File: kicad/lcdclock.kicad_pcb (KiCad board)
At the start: 2 copper layers, 102 x 102 mm, 25 parts, among them CON1 AVR-ISP, SW1 RESET, U1 ATTINY24A, U2 AY0438, U3 AY0438, U4 LCD_DE377, U5 CONRAD_DCF, Y1 32.768kHz/12.5pF

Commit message: Route PCB
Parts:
- moved C4 99.1 mm to (70.7, 38.8), turned to 180 degrees
- moved C2 90.5 mm to (46.0, 54.5), turned to 270 degrees
- moved C3 54.9 mm to (123.2, 99.8), turned to 270 degrees
- moved SW1 52.9 mm to (128.5, 63.5), turned to 0 degrees
- moved TP1 44.1 mm to (60.8, 60.8)
- moved TP3 33.0 mm to (66.0, 60.8)
- moved TP2 31.1 mm to (71.2, 60.8)
- moved TP5 19.6 mm to (48.8, 95.2)
- moved U3 13.4 mm to (120.5, 98.2)
- moved U2 11.8 mm to (48.7, 56.2)
- moved C5 7.42 mm to (48.8, 86.0), turned to 90 degrees
- moved TP6 7.29 mm to (65.8, 77.2)
- moved TP4 6.77 mm to (46.0, 81.2)
- moved CON1 6.64 mm to (127.2, 72.8), turned to 270 degrees
- moved D1 4.24 mm to (50.0, 66.0)
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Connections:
- U1 pad 11: Net-(TP3-Pad1) -> Net-(TP2-Pad1)
- U1 pad 12: Net-(TP2-Pad1) -> Net-(TP3-Pad1)
- U4 pad 29: Net-(U3-Pad20) -> Net-(U3-Pad11)
- U4 pad 31: Net-(U3-Pad19) -> Net-(U3-Pad12)
- U4 pad 32: Net-(U3-Pad18) -> Net-(U3-Pad13)
- U4 pad 33: Net-(U3-Pad17) -> Net-(U3-Pad14)
- U4 pad 35: Net-(U3-Pad16) -> Net-(U3-Pad15)
- U4 pad 36: Net-(U3-Pad15) -> Net-(U3-Pad16)
- U4 pad 37: Net-(U3-Pad14) -> Net-(U3-Pad17)
- U4 pad 38: Net-(U3-Pad13) -> Net-(U3-Pad18)
- U4 pad 39: Net-(U3-Pad12) -> Net-(U3-Pad19)
- U4 pad 40: Net-(U3-Pad11) -> Net-(U3-Pad20)
- U4 pad 67: Net-(U2-Pad20) -> Net-(U2-Pad10)
- U4 pad 68: Net-(U2-Pad19) -> Net-(U2-Pad11)
- U4 pad 70: Net-(U2-Pad18) -> Net-(U2-Pad12)
- U4 pad 72: Net-(U2-Pad17) -> Net-(U2-Pad13)
- U4 pad 73: Net-(U2-Pad16) -> Net-(U2-Pad14)
- U4 pad 76: Net-(U2-Pad14) -> Net-(U2-Pad16)
- U4 pad 77: Net-(U2-Pad13) -> Net-(U2-Pad17)
- U4 pad 78: Net-(U2-Pad12) -> Net-(U2-Pad18)
- U4 pad 79: Net-(U2-Pad11) -> Net-(U2-Pad19)
- U4 pad 80: Net-(U2-Pad10) -> Net-(U2-Pad20)
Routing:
- net Net-(U3-Pad30): track 0.00 -> 220.6 mm, vias 0 -> 5
- net +BATT: track 4.19 -> 193.1 mm
- net Net-(TP3-Pad1): track 7.76 -> 134.0 mm, vias 0 -> 8
- net Net-(U2-Pad35): track 0.00 -> 102.2 mm, vias 0 -> 6
- net Net-(TP1-Pad1): track 0.00 -> 100.0 mm, vias 0 -> 4
- net Net-(U2-Pad30): track 0.00 -> 97.1 mm, vias 0 -> 4
- net Net-(CON1-Pad1): track 0.00 -> 55.3 mm
- net Net-(CON1-Pad4): track 0.00 -> 54.9 mm
- net Net-(CON1-Pad5): track 29.3 -> 83.7 mm, vias 0 -> 1
- net GND: track 2.00 -> 56.2 mm, vias 1 -> 9
- net Net-(TP2-Pad1): track 0.00 -> 53.6 mm
- net Net-(U3-Pad20): track 0.00 -> 49.5 mm
- net Net-(U3-Pad18): track 0.00 -> 49.5 mm
- net Net-(U3-Pad19): track 0.00 -> 49.5 mm
- net Net-(U3-Pad15): track 0.00 -> 49.5 mm
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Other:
- rule pad_to_mask_clearance: 0.2 -> 0.1

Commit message: Place components on PCB
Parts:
- removed C2: 100n, Resistors_SMD:R_0805_HandSoldering
- removed CON1: AVR-ISP, Connectors:IDC_Header_Straight_6pins
- removed R2, R3: 0, Resistors_SMD:R_0805_HandSoldering
- removed TP1: DLOA, Measurement_Points:Measurement_Point_Round-SMD-Pad_Big
- removed TP2: DDAT, Measurement_Points:Measurement_Point_Round-SMD-Pad_Big
- removed TP3: DCLK, Measurement_Points:Measurement_Point_Round-SMD-Pad_Big
- removed TP4: TVCC, Measurement_Points:Measurement_Point_Round-SMD-Pad_Big
- removed TP5: TSIG, Measurement_Points:Measurement_Point_Round-SMD-Pad_Big
- removed TP6: CLK, Measurement_Points:Measurement_Point_Round-SMD-Pad_Big
- removed U5: CONRAD_DCF, LCD Clock:CONNECTOR_4x1
- added C10: 100n, Resistors_SMD:R_0805_HandSoldering, F.Cu at (48.5, 56.5)
- added C11: 15p, Resistors_SMD:R_0805_HandSoldering, F.Cu at (21.8, 36.0)
- added C12: 15p, Resistors_SMD:R_0805_HandSoldering, F.Cu at (21.8, 44.0)
- added C13: 2.2u, Resistors_SMD:R_0805_HandSoldering, F.Cu at (49.0, 32.8)
- added C14: 1u, Resistors_SMD:R_0805_HandSoldering, F.Cu at (43.5, 32.8)
- added C6: 100n, Resistors_SMD:R_0805_HandSoldering, F.Cu at (38.5, 49.5)
- added C7: 100n, Resistors_SMD:R_0805_HandSoldering, F.Cu at (31.2, 35.0)
- added C8: 100n, Resistors_SMD:R_0805_HandSoldering, F.Cu at (29.2, 42.2)
- added C9: 1u, Resistors_SMD:R_0805_HandSoldering, F.Cu at (29.2, 47.0)
- added J1: Conn_JLink_SWD, Connectors:IDC_Header_Straight_20pins, F.Cu at (56.5, 55.6)
- BT1: value 3.6V Lithium AA -> 4xAA 6.4-3.2V
- C1: value 100n -> 10u
- C4: value 120p -> 100n
- D1: value BAT60A -> LED; footprint Diodes_SMD:D_SOD-323_HandSoldering -> LCD Clock:CONNECTOR_2x1
- L1: footprint LCD Clock:WE_470uH_Inductor -> Resistors_SMD:R_1812_HandSoldering
- R1: value 10k -> 100k
- SW1: value RESET -> SW_Push; footprint Buttons_Switches_SMD:SW_SPST_PTS645 -> Buttons_Switches_SMD:SW_SPST_B3S-1000
- U1: value ATTINY24A -> STM32L073xx_48; footprint Housings_SOIC:SOIC-14_3.9x8.7mm_Pitch1.27mm -> Housings_QFP:LQFP-48_7x7mm_Pitch0.5mm
- U2: value AY0438 -> ELV_DCF-2; footprint Housings_DIP:DIP-40_W15.24mm -> LCD Clock:CONNECTOR_3x1
- U3: value AY0438 -> TPS70630; footprint Housings_DIP:DIP-40_W15.24mm -> TO_SOT_Packages_SMD:SOT-23-5_HandSoldering
- U4: value LCD_DE377 -> LCD; footprint LCD Clock:LCD-DIP -> Connectors:IDC_Header_Straight_16pins; moved to F.Cu
- Y1: value 32.768kHz/12.5pF -> 32.768kHz 12.5pF; footprint LCD Clock:MS1V-T1K -> Crystals:Crystal_SMD_SeikoEpson_MC405-2pin_9.6x4.1mm_HandSoldering
- moved U3 101.0 mm to (46.0, 30.0)
- moved C3 99.9 mm to (44.0, 39.0), turned to 0 degrees
- moved SW1 73.5 mm to (55.0, 65.2)
- moved L1 61.7 mm to (40.5, 25.5), turned to 90 degrees
- moved C5 61.6 mm to (37.0, 25.5)
- moved U4 57.5 mm to (26.2, 65.5), turned to 0 degrees
- moved U1 55.3 mm to (36.0, 41.5)
- moved Y1 54.0 mm to (25.2, 40.0), turned to 270 degrees
- moved C1 51.3 mm to (40.8, 34.5), turned to 270 degrees
- moved BT1 46.3 mm to (46.8, 22.2), turned to 270 degrees
- moved R1 43.2 mm to (37.0, 55.5), turned to 270 degrees
- moved C4 37.5 mm to (33.5, 33.5), turned to 90 degrees
- moved U2 32.3 mm to (34.2, 27.3)
- moved D1 18.4 mm to (34.2, 56.5), turned to 90 degrees
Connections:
- C1 pad 1: +BATT -> VCC
- C3 pad 1: +BATT -> VCC
- C4 pad 1: Net-(C4-Pad1) -> VCC
- D1 pad 1: +BATT -> GND
- D1 pad 2: Net-(BT1-Pad1) -> Net-(D1-Pad2)
- R1 pad 1: +BATT -> Net-(D1-Pad2)
- R1 pad 2: Net-(CON1-Pad5) -> Net-(R1-Pad2)
- SW1 pad 2: Net-(CON1-Pad5) -> Net-(C10-Pad2)
- U1 pad 1: +BATT -> VCC
- U1 pad 10: Net-(TP5-Pad1) -> (no net)
- U1 pad 11: Net-(TP2-Pad1) -> Net-(U1-Pad11)
- U1 pad 12: Net-(TP3-Pad1) -> Net-(U1-Pad12)
- U1 pad 13: Net-(TP1-Pad1) -> Net-(U1-Pad13)
- U1 pad 14: GND -> Net-(L1-Pad1)
- U1 pad 2: Net-(R3-Pad2) -> (no net)
- U1 pad 3: Net-(R2-Pad2) -> Net-(C11-Pad1)
- U1 pad 4: Net-(CON1-Pad5) -> Net-(C12-Pad1)
- U1 pad 5: Net-(TP6-Pad1) -> (no net)
- U1 pad 6: Net-(L1-Pad1) -> (no net)
- U1 pad 7: Net-(CON1-Pad4) -> Net-(C10-Pad2)
- U1 pad 8: Net-(CON1-Pad1) -> GND
- U1 pad 9: Net-(CON1-Pad3) -> VCC
- U2 pad 1: +BATT -> Net-(C5-Pad2)
- U2 pad 2: Net-(TP1-Pad1) -> Net-(U1-Pad15)
- U2 pad 3: (no net) -> GND
- U3 pad 1: +BATT -> Net-(BT1-Pad1)
- U3 pad 2: Net-(TP1-Pad1) -> GND
- U3 pad 3: (no net) -> Net-(BT1-Pad1)
- U3 pad 5: (no net) -> VCC
- U4 pad 1: Net-(U3-Pad30) -> Net-(U1-Pad11)
- U4 pad 10: Net-(U3-Pad27) -> Net-(U1-Pad41)
- U4 pad 11: Net-(U3-Pad26) -> Net-(U1-Pad21)
- U4 pad 12: Net-(U3-Pad25) -> Net-(U1-Pad22)
- U4 pad 13: (no net) -> Net-(U1-Pad46)
- U4 pad 14: (no net) -> Net-(U1-Pad31)
- U4 pad 15: (no net) -> Net-(U1-Pad30)
- U4 pad 16: (no net) -> Net-(U1-Pad29)
- U4 pad 2: Net-(U3-Pad30) -> Net-(U1-Pad12)
- U4 pad 3: Net-(U3-Pad39) -> Net-(U1-Pad13)
- U4 pad 4: Net-(U3-Pad38) -> Net-(U1-Pad16)
- U4 pad 5: Net-(U3-Pad37) -> Net-(U1-Pad17)
- U4 pad 6: Net-(U3-Pad33) -> Net-(U1-Pad18)
- U4 pad 7: Net-(U3-Pad32) -> Net-(U1-Pad19)
- U4 pad 8: Net-(U3-Pad29) -> Net-(U1-Pad39)
- U4 pad 9: Net-(U3-Pad28) -> Net-(U1-Pad40)
- Y1 pad 1: Net-(R3-Pad2) -> Net-(C11-Pad1)
- Y1 pad 2: Net-(R2-Pad2) -> Net-(C12-Pad1)
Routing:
- net Net-(U3-Pad30): track 220.6 -> 0.00 mm, vias 5 -> 0
- net +BATT: track 193.1 -> 0.00 mm
- net Net-(TP3-Pad1): track 134.0 -> 0.00 mm, vias 8 -> 0
- net Net-(U2-Pad35): track 102.2 -> 0.00 mm, vias 6 -> 0
- net Net-(TP1-Pad1): track 100.0 -> 0.00 mm, vias 4 -> 0
- net Net-(U2-Pad30): track 97.1 -> 0.00 mm, vias 4 -> 0
- net Net-(CON1-Pad5): track 83.7 -> 0.00 mm, vias 1 -> 0
- net GND: track 56.2 -> 0.00 mm, vias 9 -> 0
- net Net-(CON1-Pad1): track 55.3 -> 0.00 mm
- net Net-(CON1-Pad4): track 54.9 -> 0.00 mm
- net Net-(TP2-Pad1): track 53.6 -> 0.00 mm
- net Net-(U3-Pad20): track 49.5 -> 0.00 mm
- net Net-(U3-Pad18): track 49.5 -> 0.00 mm
- net Net-(U3-Pad19): track 49.5 -> 0.00 mm
- net Net-(U3-Pad15): track 49.5 -> 0.00 mm
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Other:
- board size 102 x 102 mm -> 41 x 50 mm

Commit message: Layout PCB
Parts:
- moved C14 7.79 mm to (44.2, 25.0), turned to 90 degrees
- moved C6 1.58 mm to (40.0, 49.0)
- moved C4 1.52 mm to (35.0, 33.8), turned to 270 degrees
- moved C13 1.50 mm to (49.0, 31.2)
- moved C3 1.50 mm to (44.0, 37.5)
- moved C10 1.41 mm to (47.5, 57.5), turned to 0 degrees
- moved U3 1.25 mm to (46.0, 31.2)
- moved C1 1.03 mm to (40.5, 33.5), turned to 180 degrees
- moved SW1 0.90 mm to (55.5, 66.0)
- moved C8 0.75 mm to (29.2, 43.0), turned to 90 degrees
- moved C9 0.75 mm to (29.2, 47.8)
- moved C7 0.50 mm to (30.8, 35.0)
- moved Y1 0.25 mm to (25.5, 40.0)
- moved J1 0.21 mm to (56.8, 55.6)
- turned C5 to 270 degrees
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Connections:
- U1 pad 14: Net-(L1-Pad1) -> (no net)
- U1 pad 15: Net-(U1-Pad15) -> (no net)
- U1 pad 42: (no net) -> Net-(L1-Pad1)
- U1 pad 43: (no net) -> Net-(U1-Pad43)
- U2 pad 2: Net-(U1-Pad15) -> Net-(U1-Pad43)
- U4 pad 14: Net-(U1-Pad31) -> Net-(U1-Pad29)
- U4 pad 16: Net-(U1-Pad29) -> Net-(U1-Pad31)
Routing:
- net VCC: track 0.00 -> 145.3 mm, vias 0 -> 4
- net Net-(C10-Pad2): track 0.00 -> 79.2 mm, vias 0 -> 2
- net GND: track 0.00 -> 44.0 mm, vias 0 -> 16
- net Net-(U1-Pad46): track 0.00 -> 34.1 mm, vias 0 -> 2
- net Net-(U1-Pad40): track 0.00 -> 30.3 mm, vias 0 -> 2
- net Net-(J1-Pad9): track 0.00 -> 29.6 mm, vias 0 -> 2
- net Net-(U1-Pad39): track 0.00 -> 28.4 mm, vias 0 -> 2
- net Net-(U1-Pad30): track 0.00 -> 27.1 mm
- net Net-(U1-Pad11): track 0.00 -> 27.1 mm, vias 0 -> 2
- net Net-(U1-Pad41): track 0.00 -> 26.8 mm, vias 0 -> 2
- net Net-(U1-Pad31): track 0.00 -> 25.2 mm
- net Net-(J1-Pad7): track 0.00 -> 24.8 mm
- net Net-(U1-Pad29): track 0.00 -> 23.7 mm
- net Net-(U1-Pad13): track 0.00 -> 23.0 mm
- net Net-(U1-Pad17): track 0.00 -> 22.3 mm
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
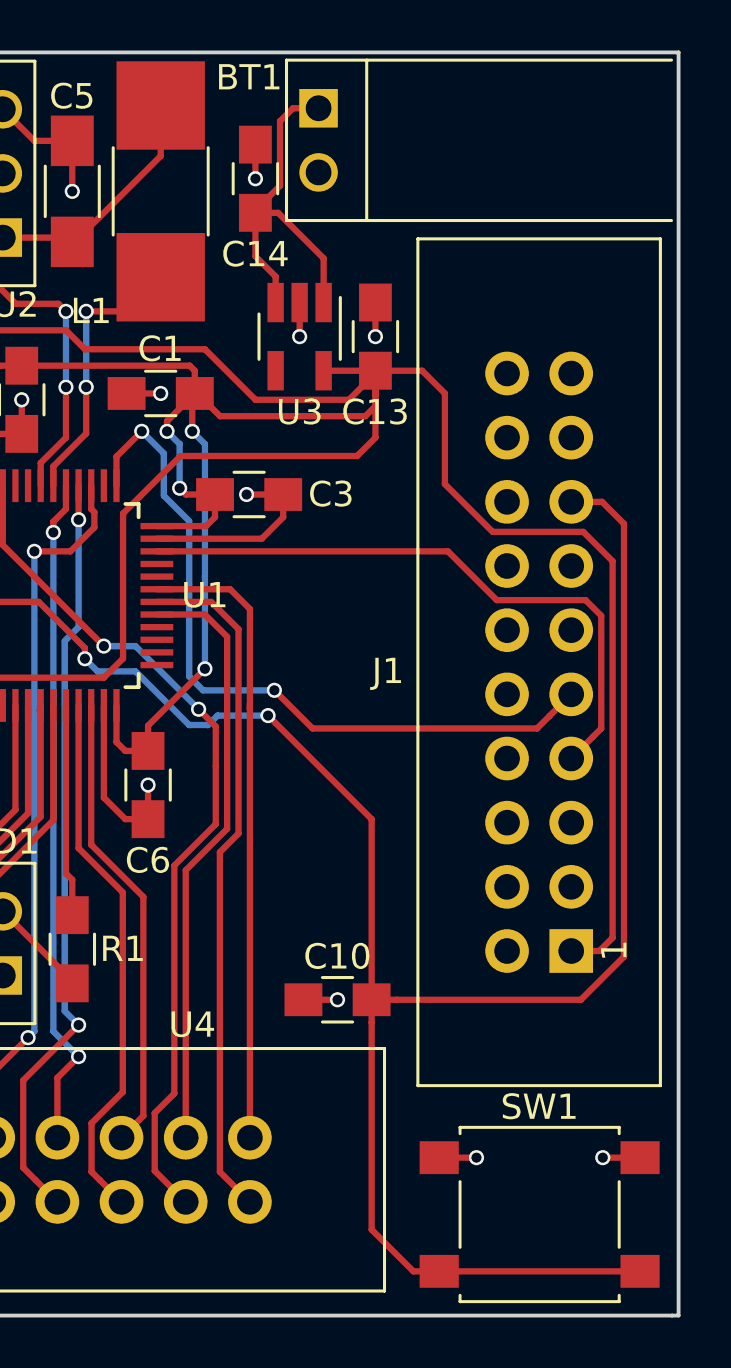
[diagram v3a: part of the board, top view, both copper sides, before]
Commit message: Add two mounting holes
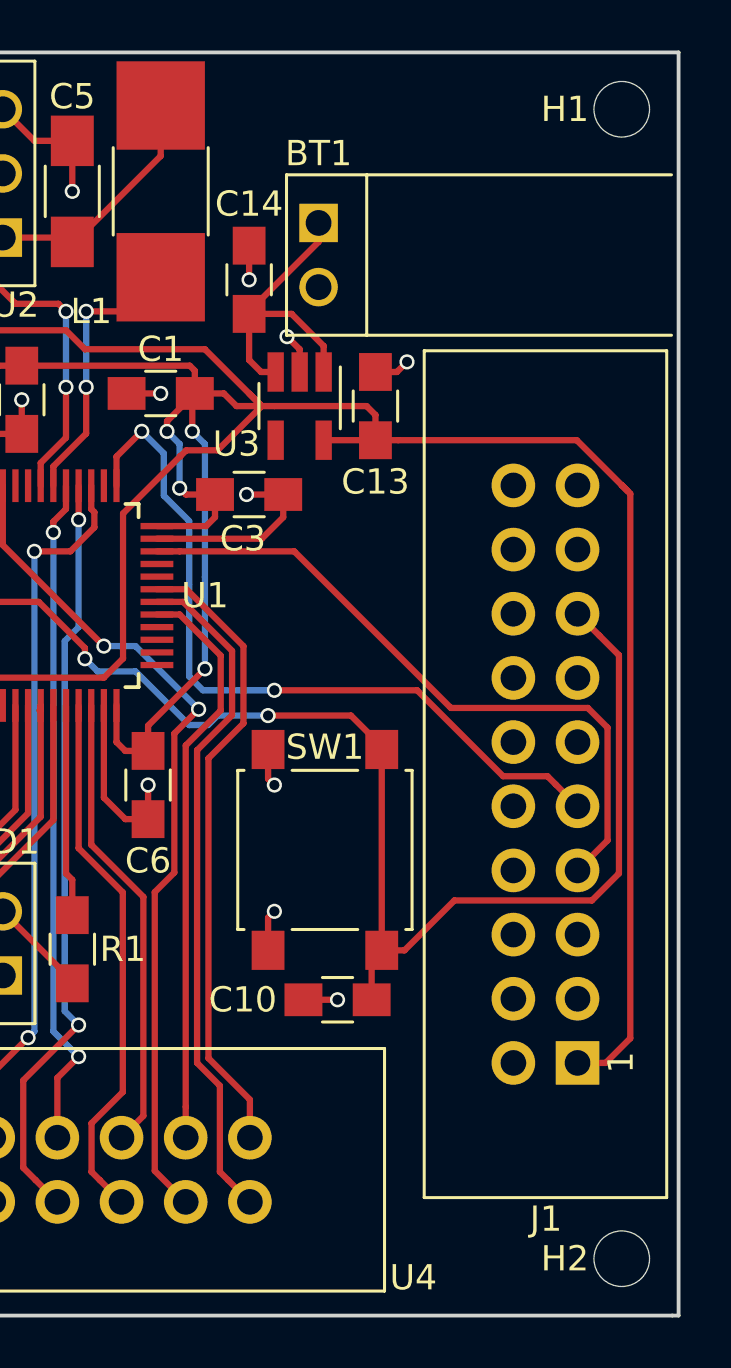
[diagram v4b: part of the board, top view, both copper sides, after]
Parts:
- added H1: MountingHole_2.2mm_M2, Mounting_Holes:MountingHole_2.2mm_M2, F.Cu at (58.8, 22.2)
- added H2: MountingHole_2.2mm_M2, Mounting_Holes:MountingHole_2.2mm_M2, F.Cu at (58.8, 67.8)
- moved SW1 16.7 mm to (47.0, 51.6), turned to 90 degrees
- moved BT1 4.54 mm to (46.8, 26.8)
- moved J1 4.44 mm to (57.0, 60.0)
- moved C14 4.01 mm to (44.0, 29.0)
- moved C13 2.75 mm to (49.0, 34.0)
- moved U3 2.75 mm to (46.0, 34.0)
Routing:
- net Net-(C10-Pad2): track 79.2 -> 52.3 mm
- net VCC: track 145.3 -> 138.4 mm
- net Net-(BT1-Pad1): track 14.8 -> 12.3 mm
- net Net-(J1-Pad7): track 24.8 -> 26.9 mm
- net Net-(J1-Pad9): track 29.6 -> 30.5 mm
- net Net-(U1-Pad29): track 23.7 -> 22.9 mm
- net Net-(U1-Pad46): track 34.1 -> 33.5 mm
- net GND: track 44.0 -> 44.6 mm
